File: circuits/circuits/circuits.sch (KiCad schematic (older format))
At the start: 68 parts

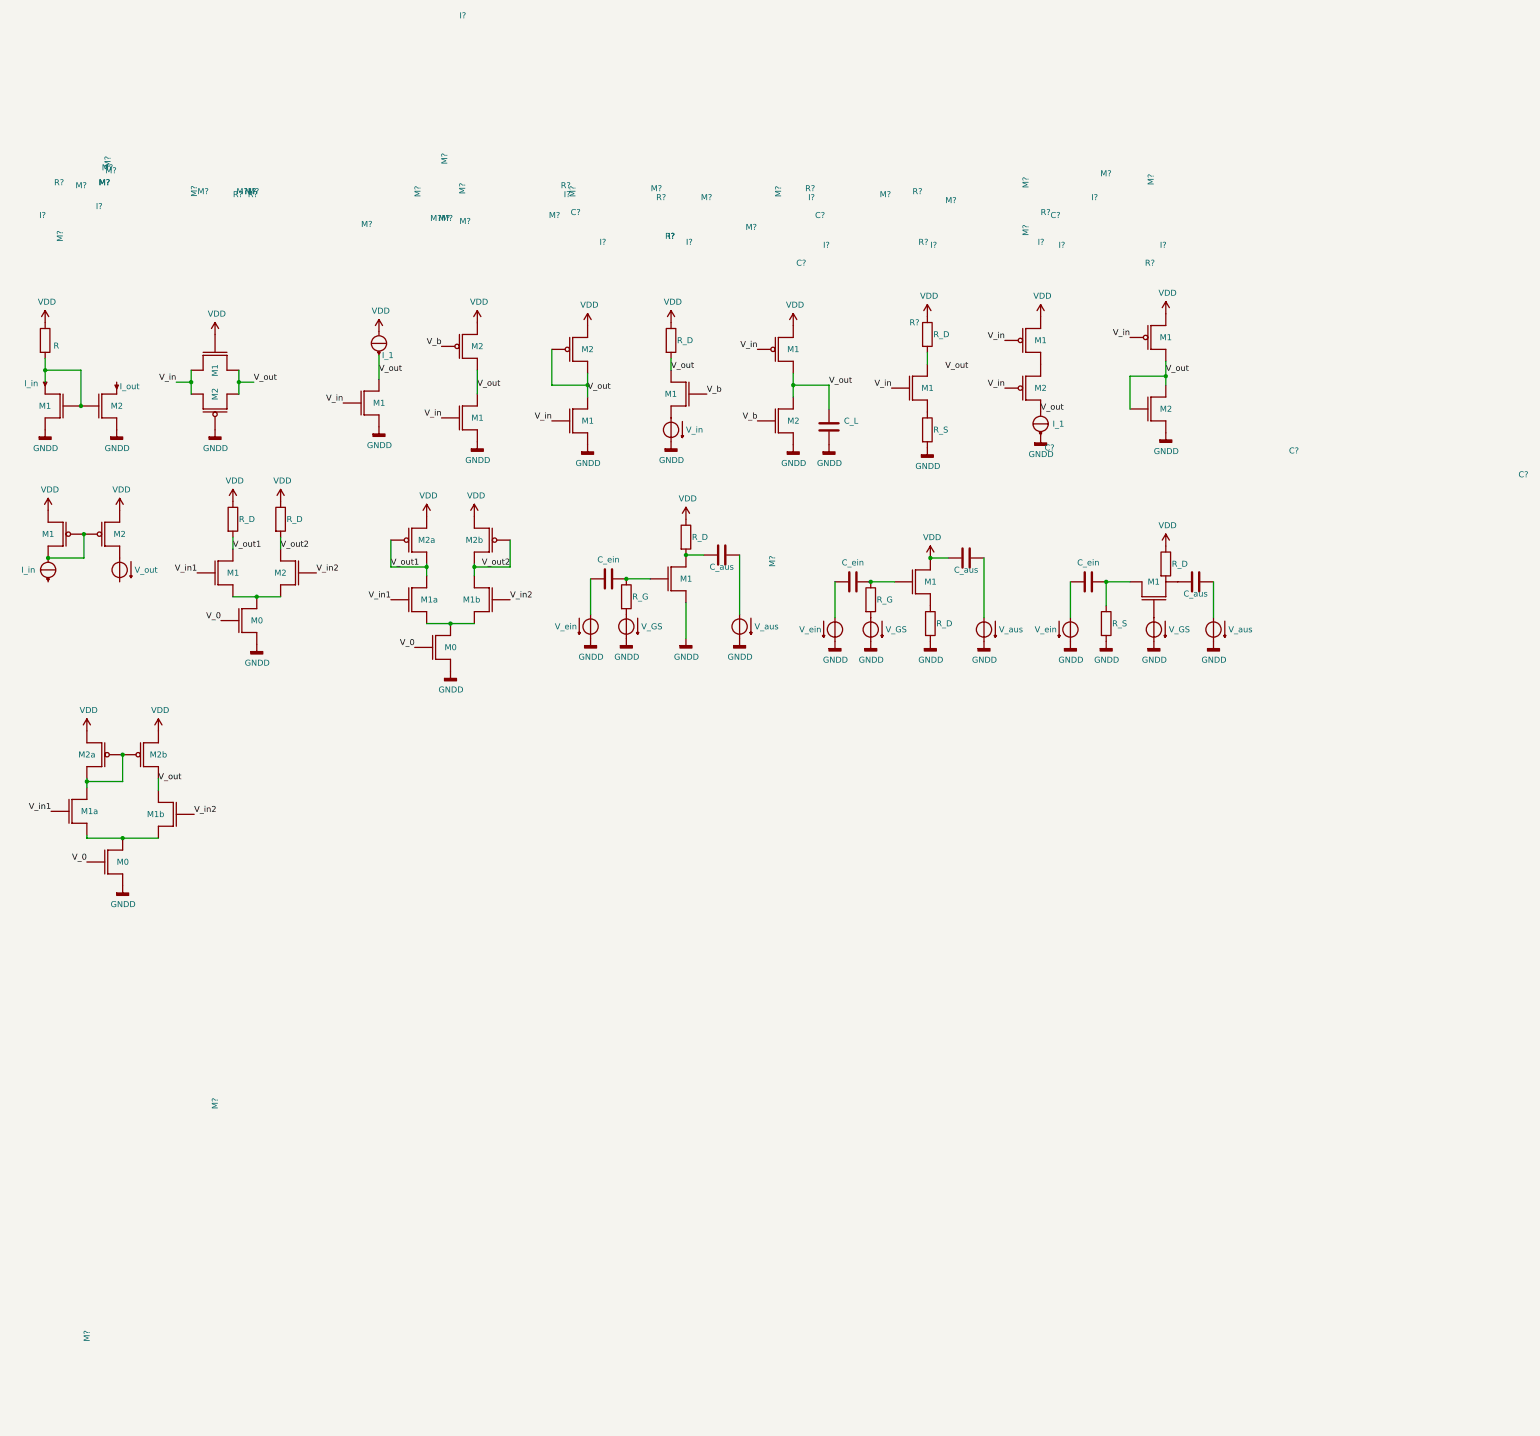
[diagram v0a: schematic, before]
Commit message: add buck, boost-buck and circuit drawings
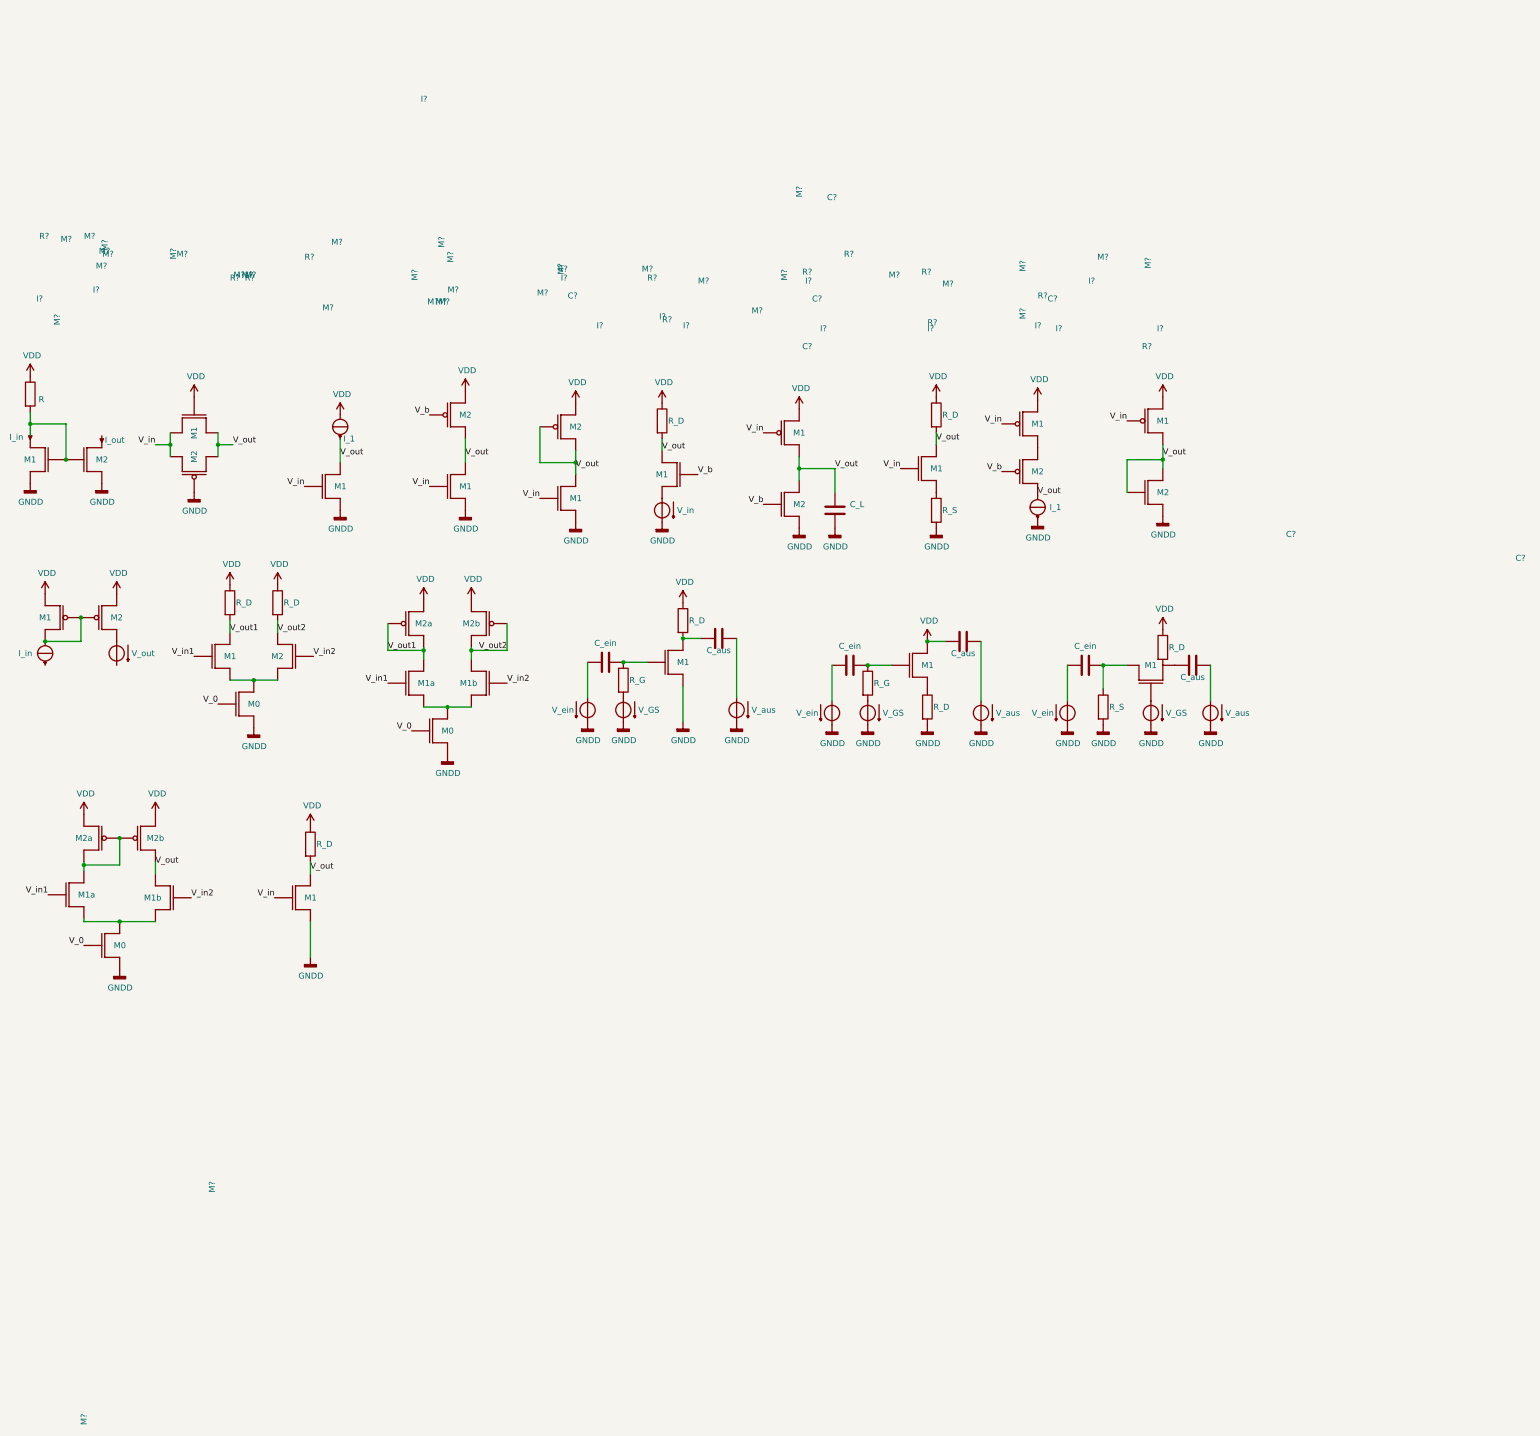
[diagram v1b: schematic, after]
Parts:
- added M?: M1, symbol pspice:MNMOS2
- added R?: R_D, symbol Device:R
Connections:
- net GNDD: now also M?.~
- net VDD: now also R?.1
- net V_b: now also M?.~
- net V_in: now also M?.~; no longer M?.~
- net V_out: now also M?.~, R?.2, M?.~, R?.2
- net at I?.~: no longer M?.~
- net at M?.~: now also C?.2; no longer I?.~
- new net: M?.~, M?.~, M?.~ (x4)
- new net: M?.~, M?.~, R?.2
- new net: I?.~, M?.~ (x3)
- new net: M?.~, M?.~
- new net: I?.~, M?.~, M?.~
- now unconnected: I?.~
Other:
- moved on the sheet: C?, I?, M?, R?
